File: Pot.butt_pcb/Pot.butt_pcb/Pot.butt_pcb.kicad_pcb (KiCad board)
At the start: 2 copper layers, 240 x 140 mm, 222 parts, among them J1 Conn_01x04_Male, J2 Conn_01x05_Male, J3 Conn_01x05_Male, M3 MountingHole_3.2mm_M3, SW1 SW_Push, SW10 SW_Push, SW11 Cherry_MX_1u, SW12 Cherry_MX_1u, SW13 Cherry_MX_1u, SW14 Cherry_MX_1u, SW15 Cherry_MX_1u, SW16 Cherry_MX_1u, SW17 Cherry_MX_1u, SW18 Cherry_MX_1u, SW19 Cherry_MX_1u, SW2 SW_DPDT, SW20 Cherry_MX_1u, SW21 Cherry_MX_1u, SW22 Cherry_MX_1u, SW23 Cherry_MX_1u, SW24 Cherry_MX_1u, SW25 Cherry_MX_1u, SW26 Cherry_MX_1u, SW27 Cherry_MX_1u, SW28 Cherry_MX_1u, SW29 Cherry_MX_1u, SW3 SW_DPDT, SW30 Cherry_MX_1u, SW31 Cherry_MX_1u, SW32 Cherry_MX_1u, SW33 Cherry_MX_1u, SW34 Cherry_MX_1u, SW35 Cherry_MX_1u, SW4 SW_DPDT, SW5 SW_DPDT, SW6 SW_DPDT, SW7 SW_DPDT, SW8 SW_DPDT, SW9 SW_DPDT, U1 STM32G030K6T6, U2 STM32G030K6T6, U3 LMR62421XMF, U4 LMR62421XMF

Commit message: Pot.butt_pcb done
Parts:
- C30: moved to B.Cu
- moved D30 76.0 mm to (241.6, 149.4)
- moved D39 76.0 mm to (165.6, 149.4)
- moved D26 38.0 mm to (222.6, 149.4)
- moved D35 38.0 mm to (184.6, 149.4)
- moved J1 1.51 mm to (111.4, 90.8)
- moved C36 1.39 mm to (214.8, 52.2), turned to -90 degrees
- moved C34 1.03 mm to (209.5, 153.9), turned to -90 degrees
- moved C40 0.98 mm to (239.7, 52.1), turned to -90 degrees
- moved C44 0.90 mm to (265.0, 52.1), turned to -90 degrees
- moved D47 0.73 mm to (259.6, 72.4)
- moved C38 0.70 mm to (227.7, 153.9), turned to -90 degrees
- moved C42 0.69 mm to (246.7, 153.9), turned to -90 degrees
- moved R19 0.66 mm to (110.6, 80.0), turned to 180 degrees
- moved C30 0.65 mm to (189.7, 153.8), turned to -90 degrees
- moved D44 0.63 mm to (209.6, 72.4)
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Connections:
- U2 pad 31: USART1_RXs -> LEDS
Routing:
- net +5V: track 0.00 -> 770.0 mm, vias 0 -> 41
- net +3V3: track 19.0 -> 519.3 mm, vias 0 -> 11
- net 3.3VA: track 0.00 -> 484.5 mm, vias 0 -> 7
- net 5th_Column: track 0.00 -> 236.8 mm, vias 0 -> 3
- net 4th_Column: track 0.00 -> 212.0 mm, vias 0 -> 3
- net 3rd_Column: track 0.00 -> 182.9 mm, vias 0 -> 3
- net 2nd_Column: track 0.00 -> 159.4 mm, vias 0 -> 3
- net 1st_Column: track 0.00 -> 133.7 mm, vias 0 -> 1
- net NRSTs: track 0.00 -> 133.3 mm, vias 0 -> 4
- net SWCLKs: track 0.00 -> 122.6 mm, vias 0 -> 2
- net SWDIOs: track 0.00 -> 120.7 mm, vias 0 -> 2
- net NRSTp: track 0.00 -> 119.0 mm, vias 0 -> 2
- net Net-(R15-Pad2): track 0.00 -> 117.6 mm
- net Net-(R14-Pad2): track 0.00 -> 117.4 mm
- net Net-(R17-Pad2): track 0.00 -> 102.2 mm
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- added copper zone on B.Cu, net GND
- added copper zone on F.Cu, net GND
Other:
- board text added: "MUTE"

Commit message: pcb design fixing
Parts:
- removed C15, C18: 100nF, Capacitor_SMD:C_0805_2012Metric_Pad1.18x1.45mm_HandSolder
- removed D56: RED LED, LED_SMD:LED_0805_2012Metric_Pad1.15x1.40mm_HandSolder
- removed the M3 at (275.0, 30.0)
- removed the M3 at (275.0, 158.0)
- removed the M3 at (48.0, 158.0)
- removed the M3 at (48.0, 30.0)
- removed R30: 1k, Resistor_SMD:R_0805_2012Metric_Pad1.20x1.40mm_HandSolder
- removed RV1, RV10, RV11, RV12, RV13, RV14, RV15, RV16, RV17, RV18, RV19, RV2, RV20, RV3, RV4, RV5, RV6, RV7, RV8, RV9: R_Potentiometer, Connector_PinSocket_2.54mm:PinSocket_1x03_P2.54mm_Vertical
- removed SW2, SW3, SW4, SW5, SW6, SW7, SW8, SW9: SW_DPDT, Connector_PinSocket_2.54mm:PinSocket_1x03_P2.54mm_Vertical
- added J4: Conn_01x40_Male, Connector_IDC:IDC-Header_2x20_P2.54mm_Vertical, F.Cu at (57.0, 37.0)
- added J5: Conn_01x40_Male, Connector_IDC:IDC-Header_2x20_P2.54mm_Vertical, F.Cu at (57.0, 103.0)
- added J6: Conn_01x40_Male, Connector_IDC:IDC-Header_2x20_P2.54mm_Vertical, F.Cu at (80.0, 146.0)
- added M3: MountingHole_3.2mm_M3, MountingHole:MountingHole_3.2mm_M3, F.Cu at (69.0, 28.0)
- added M3: MountingHole_3.2mm_M3, MountingHole:MountingHole_3.2mm_M3, F.Cu at (198.0, 27.0)
- added M3: MountingHole_3.2mm_M3, MountingHole:MountingHole_3.2mm_M3, F.Cu at (198.0, 160.0)
- added M3: MountingHole_3.2mm_M3, MountingHole:MountingHole_3.2mm_M3, F.Cu at (275.0, 28.0)
- added M3: MountingHole_3.2mm_M3, MountingHole:MountingHole_3.2mm_M3, F.Cu at (69.0, 160.0)
- added M3: MountingHole_3.2mm_M3, MountingHole:MountingHole_3.2mm_M3, F.Cu at (275.0, 160.0)
- C1, C10, C11, C12, C13, C19, C20, C21, C22, C23, C24, C25, C26, C3, C4, C5, C6, C7, C8, C9, R4, R5, R6, R7, R8: moved to B.Cu
- D53, D55: value GREEN LED -> RED LED
- D54: value RED LED -> GREEN LED
- J1: value Conn_01x04_Male -> Conn_01x10_Male; footprint Connector_PinSocket_2.54mm:PinSocket_1x04_P2.54mm_Vertical -> Connector_IDC:IDC-Header_2x05_P2.54mm_Horizontal
- R1, R2, R3: value 100 -> 1k
- R19: value 100k -> 10k; moved to B.Cu
- R20: value 100k -> 10k
- R27, R28, R29: value 1k -> 100; moved to B.Cu
- moved D54 122.7 mm to (148.6, 147.5)
- moved C23 103.2 mm to (67.3, 48.6)
- moved R29 101.3 mm to (118.1, 135.5), turned to -90 degrees
- moved C22 101.2 mm to (67.4, 63.9), turned to 90 degrees
- moved C24 100.3 mm to (67.5, 69.0), turned to 90 degrees
- moved J3 97.2 mm to (127.0, 92.5), turned to 90 degrees
- moved C21 95.7 mm to (67.3, 43.6)
- moved C20 93.4 mm to (67.4, 58.8), turned to 90 degrees
- moved R3 91.6 mm to (125.1, 74.4)
- moved C19 88.8 mm to (67.2, 38.5)
- moved D55 87.6 mm to (129.5, 74.4)
- moved C7 87.3 mm to (66.3, 119.8), turned to 90 degrees
- moved C26 86.2 mm to (67.3, 53.7), turned to 90 degrees
- moved C25 82.0 mm to (67.5, 74.1), turned to 90 degrees
- moved R27 80.1 mm to (113.0, 135.5), turned to -90 degrees
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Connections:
- net ADC_in15p renamed ADC_in11p
- C10 pad 1: ADC_in2p -> ADC_in6p
- C11 pad 1: ADC_in6p -> ADC_in10p
- C12 pad 1: ADC_in10p -> ADC_in3p
- C3 pad 1: +3V3 -> ADC_in0p
- C4 pad 1: ADC_in0p -> ADC_in4p
- C5 pad 1: ADC_in4p -> ADC_in8p
- C6 pad 1: ADC_in8p -> ADC_in1p
- C7 pad 1: ADC_in1p -> ADC_in5p
- C8 pad 1: ADC_in5p -> ADC_in9p
- C9 pad 1: ADC_in9p -> ADC_in2p
- D53 pad 1: Net-(D53-Pad1) -> GND
- D53 pad 2: +3V3 -> Net-(D53-Pad2)
- D55 pad 1: Net-(D55-Pad1) -> GND
- D55 pad 2: +3V3 -> Net-(D55-Pad2)
- J1 pad 1: I2C1_SCL -> LOAD
- J1 pad 2: I2C1_SDA -> GND
- R1 pad 1: SW1p -> STATUS_LEDp
- R1 pad 2: Net-(R1-Pad2) -> Net-(D53-Pad2)
- R2 pad 1: SW5p -> LOAD
- R2 pad 2: Net-(R2-Pad2) -> Net-(D54-Pad2)
- R27 pad 1: USART1_TXp -> SW7p
- R27 pad 2: Net-(D53-Pad1) -> SW7
- R28 pad 1: USART1_TXp -> SW4p
- R28 pad 2: Net-(D54-Pad2) -> SW4
- R29 pad 1: USART1_TXs -> SW8p
- R29 pad 2: Net-(D55-Pad1) -> SW8
- R3 pad 1: SW2p -> STATUS_LEDs
- R3 pad 2: Net-(R3-Pad2) -> Net-(D55-Pad2)
- R4 pad 1: SW6p -> SW1p
- R4 pad 2: Net-(R4-Pad2) -> SW1
- R5 pad 1: SW3p -> SW5p
- R5 pad 2: Net-(R5-Pad2) -> SW5
- R6 pad 1: SW7p -> SW2p
- R6 pad 2: Net-(R6-Pad2) -> SW2
- R7 pad 1: SW4p -> SW6p
- R7 pad 2: Net-(R7-Pad2) -> SW6
- R8 pad 1: SW8p -> SW3p
- R8 pad 2: Net-(R8-Pad2) -> SW3
- U1 pad 1: SW8p -> STATUS_LEDp
- U1 pad 2: SW7p -> unconnected-(U1-Pad2)
- U1 pad 30: USART1_TXp -> SW6p
- U1 pad 31: USART1_RXp -> SW7p
- U1 pad 32: SW6p -> SW8p
- U2 pad 15: ADC_in8s -> unconnected-(U2-Pad15)
- U2 pad 16: ADC_in9s -> unconnected-(U2-Pad16)
- U2 pad 17: ADC_in10s -> unconnected-(U2-Pad17)
- U2 pad 3: unconnected-(U2-Pad3) -> STATUS_LEDs
- U2 pad 30: USART1_TXs -> unconnected-(U2-Pad30)
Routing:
- net 3.3VA: track 484.5 -> 269.2 mm, vias 7 -> 2
- net +3V3: track 519.3 -> 328.5 mm, vias 11 -> 7
- net SWCLKs: track 122.6 -> 13.7 mm, vias 2 -> 1
- net SWDIOs: track 120.7 -> 18.8 mm, vias 2 -> 1
- net USART1_TXs: track 98.0 -> 0.00 mm, vias 2 -> 0
- net LOAD: track 90.2 -> 169.6 mm
- net GND: track 81.3 -> 9.20 mm, vias 2354 -> 1037
- net USART1_TXp: track 70.5 -> 0.00 mm, vias 2 -> 0
- net NRSTp: track 119.0 -> 56.9 mm
- net I2C1_SDA: track 63.5 -> 123.1 mm, vias 3 -> 2
- net I2C1_SCL: track 65.6 -> 123.3 mm, vias 3 -> 2
- net NRSTs: track 133.3 -> 76.8 mm, vias 4 -> 3
- net ADC_in1p: track 104.6 -> 53.6 mm, vias 2 -> 1
- net ADC_in0p: track 99.0 -> 56.6 mm
- net ADC_in0s: track 41.5 -> 80.2 mm, vias 0 -> 1
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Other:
- board size 240 x 140 mm -> 230 x 142 mm

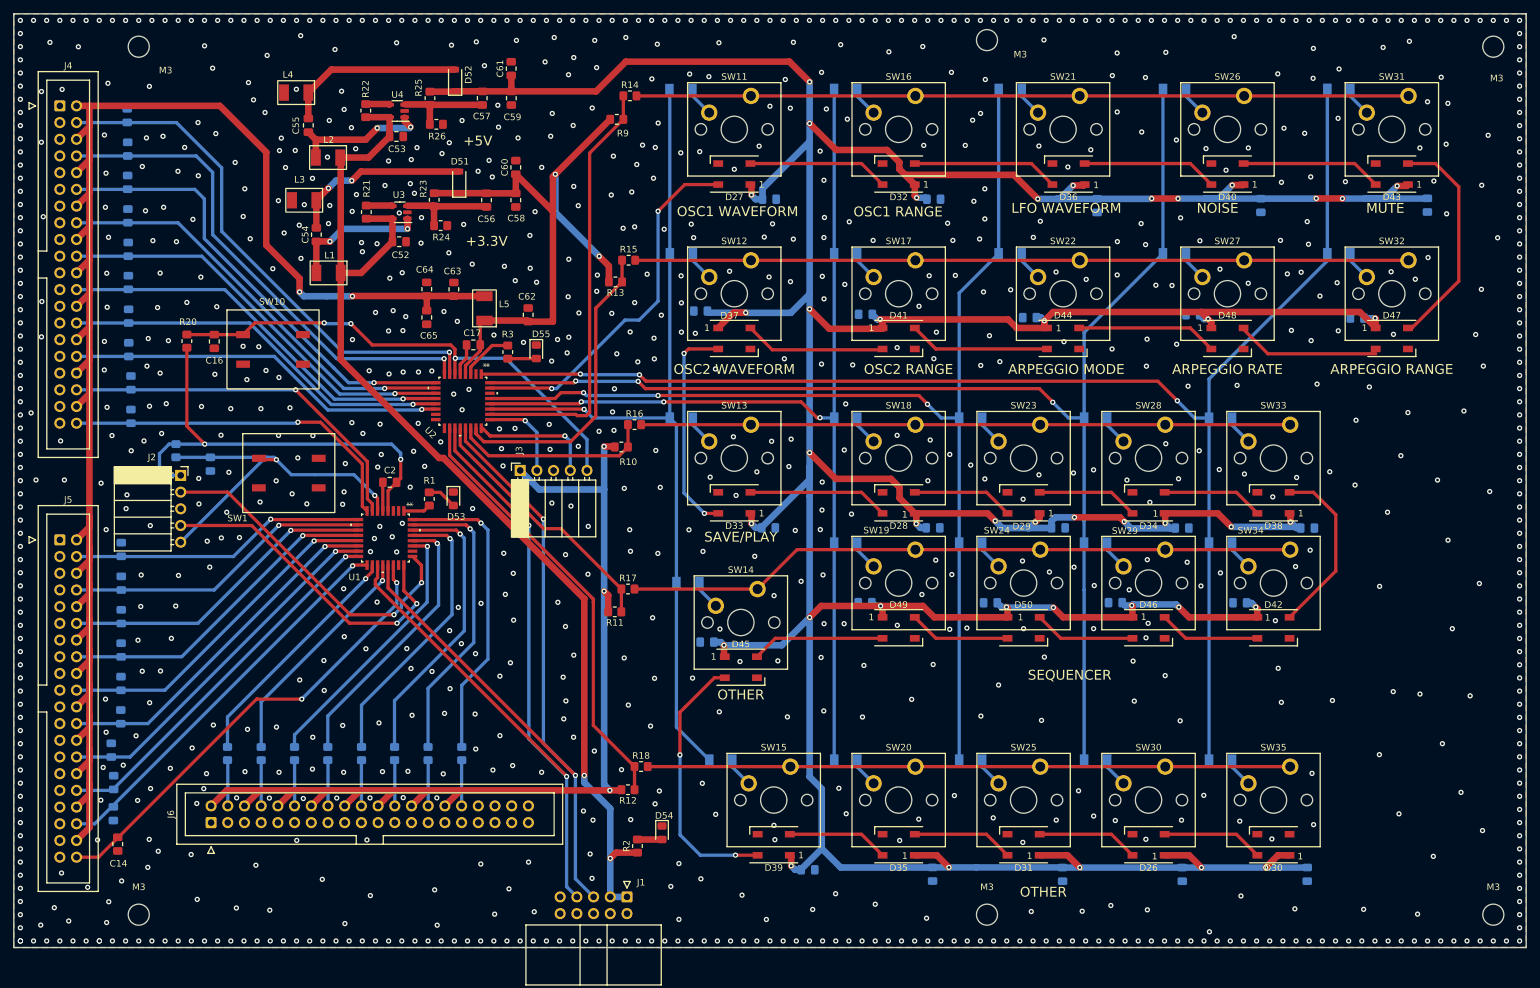
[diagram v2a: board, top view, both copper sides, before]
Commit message: pcb mounting hole change
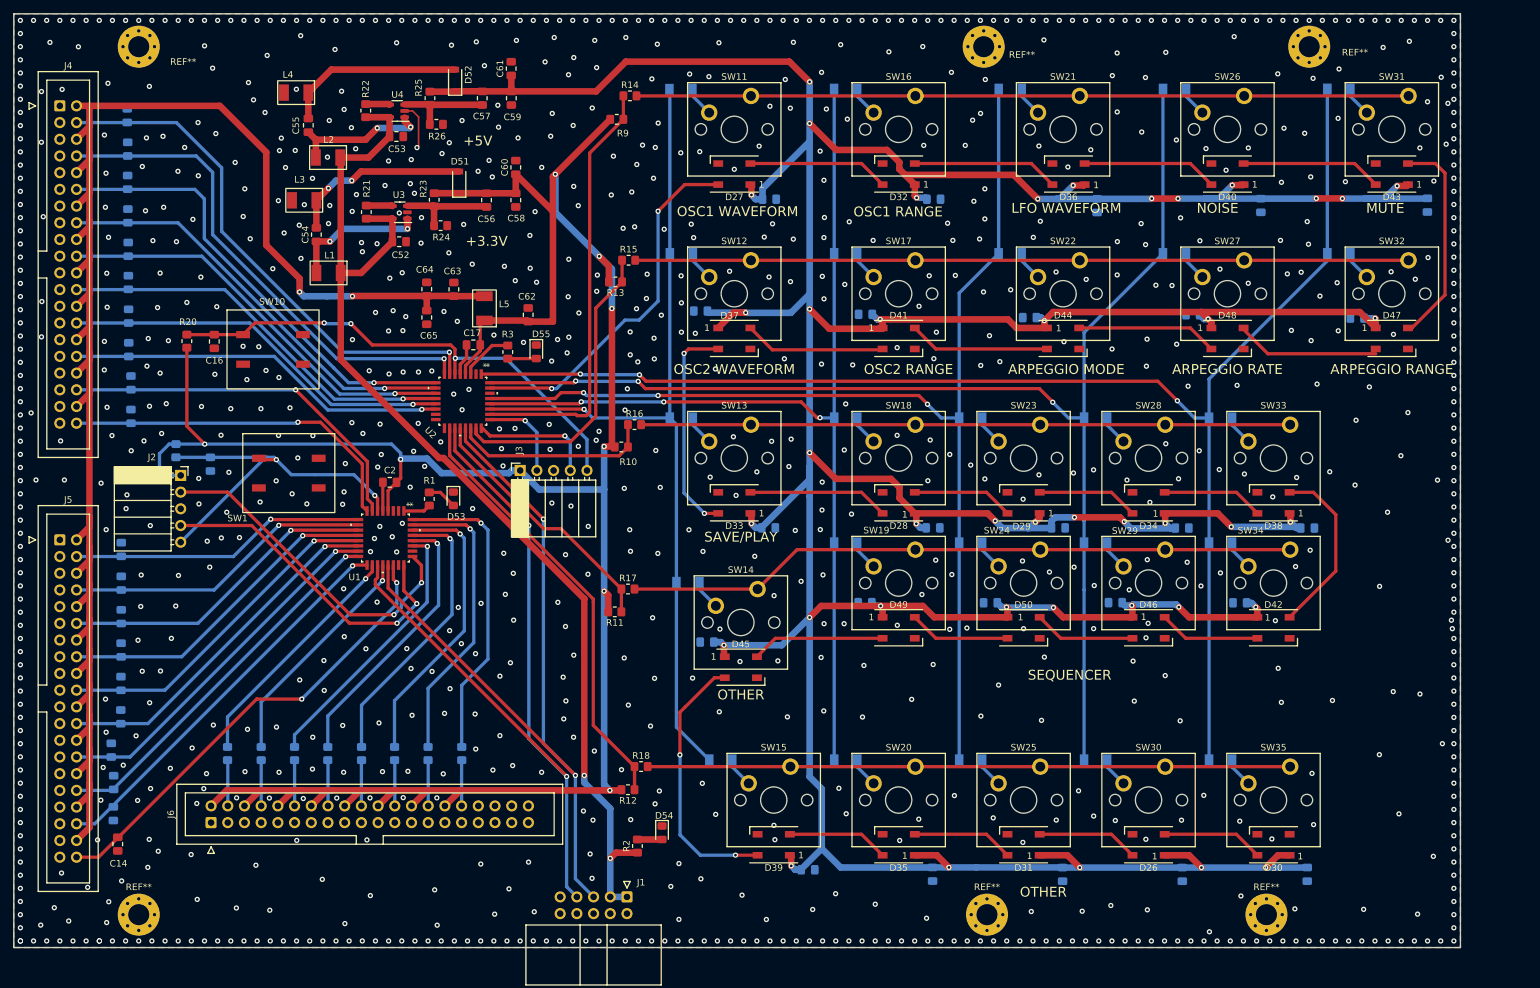
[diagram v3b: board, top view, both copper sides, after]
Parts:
- removed M3 (x6): MountingHole_3.2mm_M3, MountingHole:MountingHole_3.2mm_M3
- added REF**: MountingHole_3.2mm_M3_Pad_Via, MountingHole:MountingHole_3.2mm_M3_Pad_Via, F.Cu at (69.0, 160.0)
- added REF**: MountingHole_3.2mm_M3_Pad_Via, MountingHole:MountingHole_3.2mm_M3_Pad_Via, F.Cu at (197.5, 28.0)
- added REF**: MountingHole_3.2mm_M3_Pad_Via, MountingHole:MountingHole_3.2mm_M3_Pad_Via, F.Cu at (240.5, 160.0)
- added REF**: MountingHole_3.2mm_M3_Pad_Via, MountingHole:MountingHole_3.2mm_M3_Pad_Via, F.Cu at (247.0, 28.0)
- added REF**: MountingHole_3.2mm_M3_Pad_Via, MountingHole:MountingHole_3.2mm_M3_Pad_Via, F.Cu at (69.0, 28.0)
- added REF**: MountingHole_3.2mm_M3_Pad_Via, MountingHole:MountingHole_3.2mm_M3_Pad_Via, F.Cu at (198.0, 160.0)
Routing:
- net +3V3: track 328.5 -> 377.8 mm, vias 7 -> 8
- net GND: track 9.20 -> 16.5 mm, vias 1037 -> 1013
- net Net-(D43-Pad2): track 34.2 -> 32.5 mm
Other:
- board size 230 x 142 mm -> 220 x 142 mm
